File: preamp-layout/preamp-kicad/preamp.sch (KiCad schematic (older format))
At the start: 2 parts, among them SW1 Rotary_Encoder_Switch, SW2 Rotary_Encoder_Switch

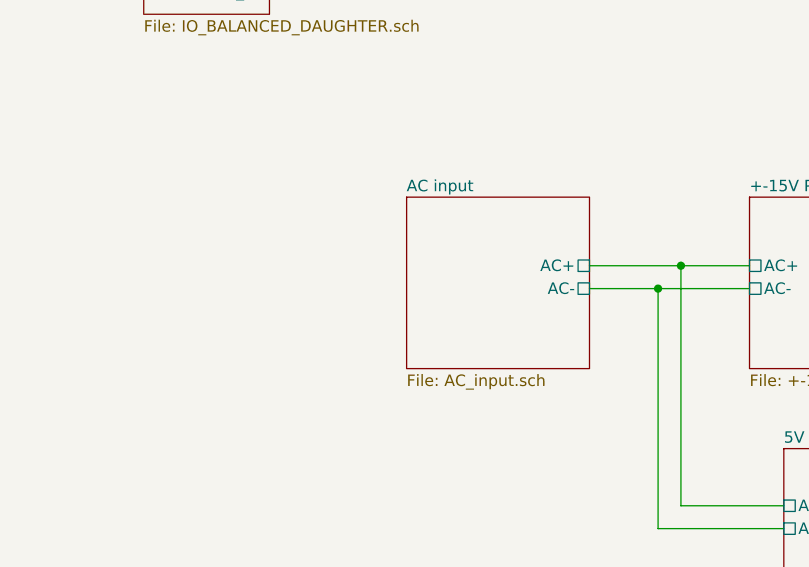
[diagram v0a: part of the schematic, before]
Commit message: AC PCB Update
Removed Switch symbol from PCB, moved to main sheet. Started playing with footprint assignment. Other minor updates.
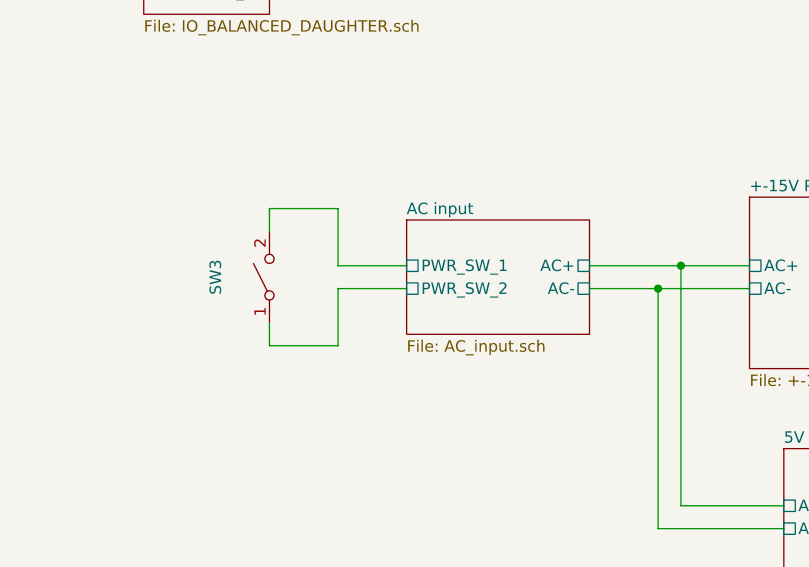
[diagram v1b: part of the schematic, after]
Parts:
- added SW3: SW_SPST, symbol Switch:SW_SPST
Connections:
- new net AC input/PWR_SW_1: SW3.2 (B)
- new net AC input/PWR_SW_2: SW3.1 (A)
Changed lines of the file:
@@
 $EndDescr
 $Sheet
-S 2550 5700 800  750
+S 2550 5800 800  500
 U 5E26F6FE
 F0 "AC input" 50
@@
 F2 "AC+" U R 3350 6000 50
 F3 "AC-" U R 3350 6100 50
+F4 "PWR_SW_1" U L 2550 6000 50
+F5 "PWR_SW_2" U L 2550 6100 50
 $EndSheet
 $Sheet
@@
 F4 "CLK" I R 5850 4150 50
 F5 "CS" I R 5850 4400 50
-F9 "LED_DT" I R 5850 4500 50
+F6 "LED_DT" I R 5850 4500 50
 $EndSheet
 $Sheet
@@
 Wire Wire Line
 	10750 2400 10750 2900
+$Comp
+L Switch:SW_SPST SW?
+U 1 1 5E2E8D21
+P 1950 6050
+AR Path="/5E26F6FE/5E2E8D21" Ref="SW?"  Part="1"
+AR Path="/5E2E8D21" Ref="SW3"  Part="1"
+F 0 "SW3" H 1950 6285 50  0000 C CNN
+F 1 "SW_SPST" H 1950 6194 50  0001 C CNN
+F 2 "" H 1950 6050 50  0001 C CNN
+F 3 "~" H 1950 6050 50  0001 C CNN
+	1    1950 6050
+	0    -1   -1   0
+$EndComp
+Wire Wire Line
+	1950 5850 1950 5750
+Wire Wire Line
+	1950 5750 2250 5750
+Wire Wire Line
+	2250 5750 2250 6000
+Wire Wire Line
+	2250 6000 2550 6000
+Wire Wire Line
+	1950 6250 1950 6350
+Wire Wire Line
+	1950 6350 2250 6350
+Wire Wire Line
+	2250 6350 2250 6100
+Wire Wire Line
+	2250 6100 2550 6100
 Wire Bus Line
 	5200 1700 5200 3300

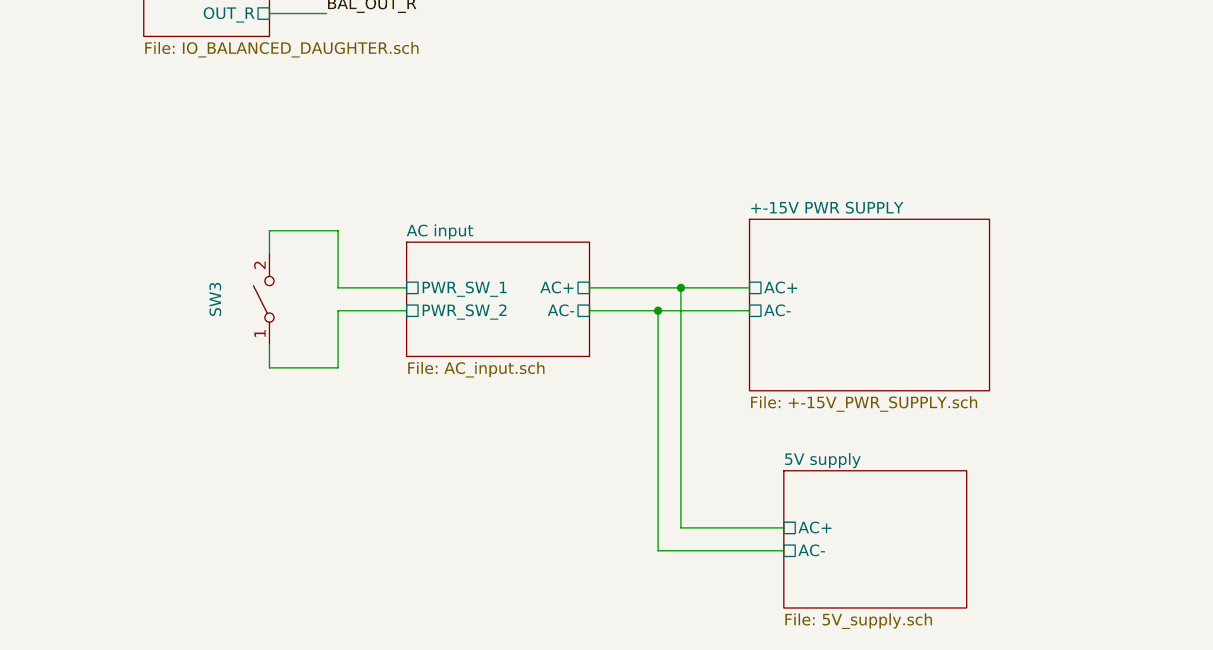
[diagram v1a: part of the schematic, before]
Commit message: Initial Footprint Assignment
Assigned footprints to SMT resistors, pin headers, screw terminals, LEDs, DIP-8 ICs
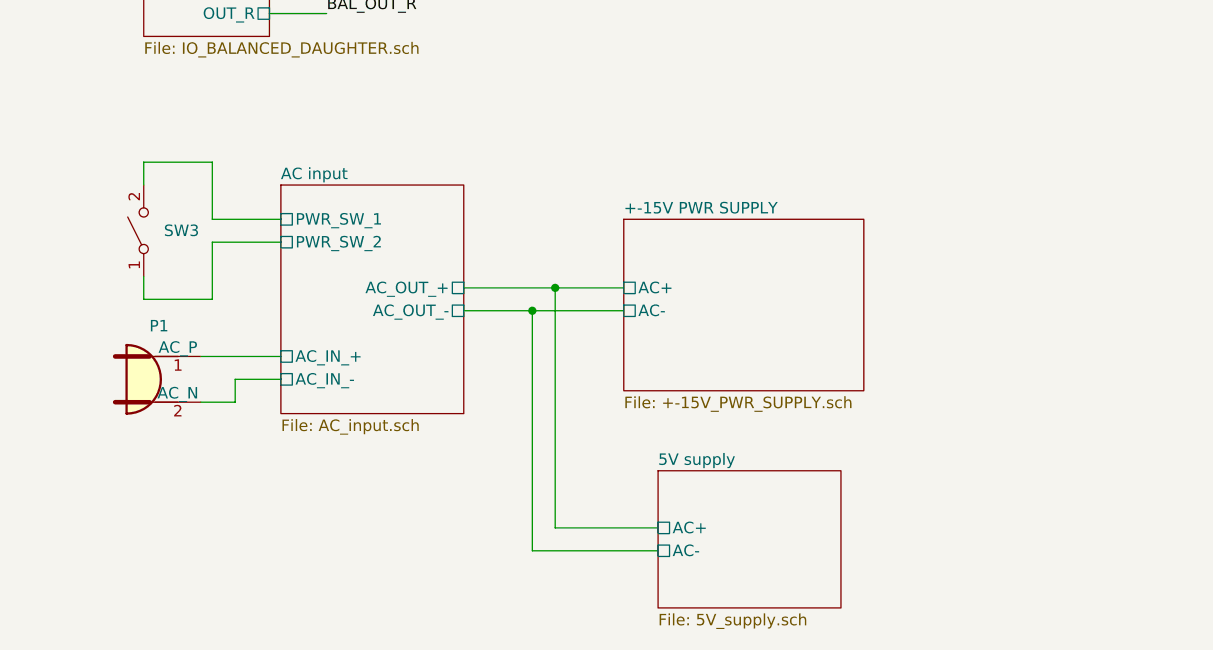
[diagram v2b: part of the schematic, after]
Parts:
- added P1: Conn_WallPlug, symbol Connector:Conn_WallPlug
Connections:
- new net AC input/AC_IN_+: P1.1 (AC_P)
- new net AC input/AC_IN_-: P1.2 (AC_N)
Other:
- moved on the sheet: SW3
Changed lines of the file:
@@
 $EndDescr
 $Sheet
-S 2550 5800 800  500
+S 2000 5550 800  1000
 U 5E26F6FE
 F0 "AC input" 50
 F1 "AC_input.sch" 50
-F2 "AC+" U R 3350 6000 50
-F3 "AC-" U R 3350 6100 50
-F4 "PWR_SW_1" U L 2550 6000 50
-F5 "PWR_SW_2" U L 2550 6100 50
-$EndSheet
-$Sheet
-S 4050 5700 1050 750
+F2 "PWR_SW_1" U L 2000 5700 50
+F3 "PWR_SW_2" U L 2000 5800 50
+F4 "AC_OUT_+" U R 2800 6000 50
+F5 "AC_IN_-" U L 2000 6400 50
+F6 "AC_IN_+" U L 2000 6300 50
+F7 "AC_OUT_-" U R 2800 6100 50
+$EndSheet
+$Sheet
+S 3500 5700 1050 750
 U 5E27B612
 F0 "+-15V PWR SUPPLY" 50
 F1 "+-15V_PWR_SUPPLY.sch" 50
-F2 "AC+" U L 4050 6000 50
-F3 "AC-" U L 4050 6100 50
-$EndSheet
-$Sheet
-S 4200 6800 800  600
+F2 "AC+" U L 3500 6000 50
+F3 "AC-" U L 3500 6100 50
+$EndSheet
+$Sheet
+S 3650 6800 800  600
 U 5E5EF2D4
 F0 "5V supply" 50
 F1 "5V_supply.sch" 50
-F2 "AC+" U L 4200 7050 50
-F3 "AC-" U L 4200 7150 50
+F2 "AC+" U L 3650 7050 50
+F3 "AC-" U L 3650 7150 50
 $EndSheet
 $Sheet
@@
 	8000 3500 8100 3600
 Wire Wire Line
-	3350 6000 3750 6000
-Wire Wire Line
-	3350 6100 3650 6100
-Wire Wire Line
-	3750 6000 3750 7050
-Wire Wire Line
-	3750 7050 4200 7050
-Connection ~ 3750 6000
-Wire Wire Line
-	3750 6000 4050 6000
-Wire Wire Line
-	3650 6100 3650 7150
-Wire Wire Line
-	3650 7150 4200 7150
-Connection ~ 3650 6100
-Wire Wire Line
-	3650 6100 4050 6100
+	2800 6000 3200 6000
+Wire Wire Line
+	2800 6100 3100 6100
+Wire Wire Line
+	3200 6000 3200 7050
+Wire Wire Line
+	3200 7050 3650 7050
+Connection ~ 3200 6000
+Wire Wire Line
+	3200 6000 3500 6000
+Wire Wire Line
+	3100 6100 3100 7150
+Wire Wire Line
+	3100 7150 3650 7150
+Connection ~ 3100 6100
+Wire Wire Line
+	3100 6100 3500 6100
 Wire Wire Line
 	1950 4450 2200 4450
@@
 L Switch:SW_SPST SW?
 U 1 1 5E2E8D21
-P 1950 6050
+P 1400 5750
 AR Path="/5E26F6FE/5E2E8D21" Ref="SW?"  Part="1"
 AR Path="/5E2E8D21" Ref="SW3"  Part="1"
-F 0 "SW3" H 1950 6285 50  0000 C CNN
-F 1 "SW_SPST" H 1950 6194 50  0001 C CNN
-F 2 "" H 1950 6050 50  0001 C CNN
-F 3 "~" H 1950 6050 50  0001 C CNN
-	1    1950 6050
+F 0 "SW3" V 1400 5662 50  0000 R CNN
+F 1 "SW_SPST" H 1400 5894 50  0001 C CNN
+F 2 "" H 1400 5750 50  0001 C CNN
+F 3 "~" H 1400 5750 50  0001 C CNN
+	1    1400 5750
 	0    -1   -1   0
 $EndComp
 Wire Wire Line
-	1950 5850 1950 5750
-Wire Wire Line
-	1950 5750 2250 5750
-Wire Wire Line
-	2250 5750 2250 6000
-Wire Wire Line
-	2250 6000 2550 6000
-Wire Wire Line
-	1950 6250 1950 6350
-Wire Wire Line
-	1950 6350 2250 6350
-Wire Wire Line
-	2250 6350 2250 6100
-Wire Wire Line
-	2250 6100 2550 6100
+	1400 5550 1400 5450
+Wire Wire Line
+	1400 5450 1700 5450
+Wire Wire Line
+	1700 5450 1700 5700
+Wire Wire Line
+	1700 5700 2000 5700
+Wire Wire Line
+	1400 5950 1400 6050
+Wire Wire Line
+	1400 6050 1700 6050
+Wire Wire Line
+	1700 6050 1700 5800
+Wire Wire Line
+	1700 5800 2000 5800
+$Comp
+L Connector:Conn_WallPlug P?
+U 1 1 5E300B43
+P 1450 6400
+AR Path="/5E26F6FE/5E300B43" Ref="P?"  Part="1"
+AR Path="/5E300B43" Ref="P1"  Part="1"
+F 0 "P1" H 1467 6633 50  0000 C CNN
+F 1 "Conn_WallPlug" H 1467 6634 50  0001 C CNN
+F 2 "" H 1850 6400 50  0001 C CNN
+F 3 "~" H 1850 6400 50  0001 C CNN
+	1    1450 6400
+	1    0    0    -1
+$EndComp
+Wire Wire Line
+	1650 6300 2000 6300
+Wire Wire Line
+	1650 6500 1800 6500
+Wire Wire Line
+	1800 6500 1800 6400
+Wire Wire Line
+	1800 6400 2000 6400
 Wire Bus Line
 	5200 1700 5200 3300

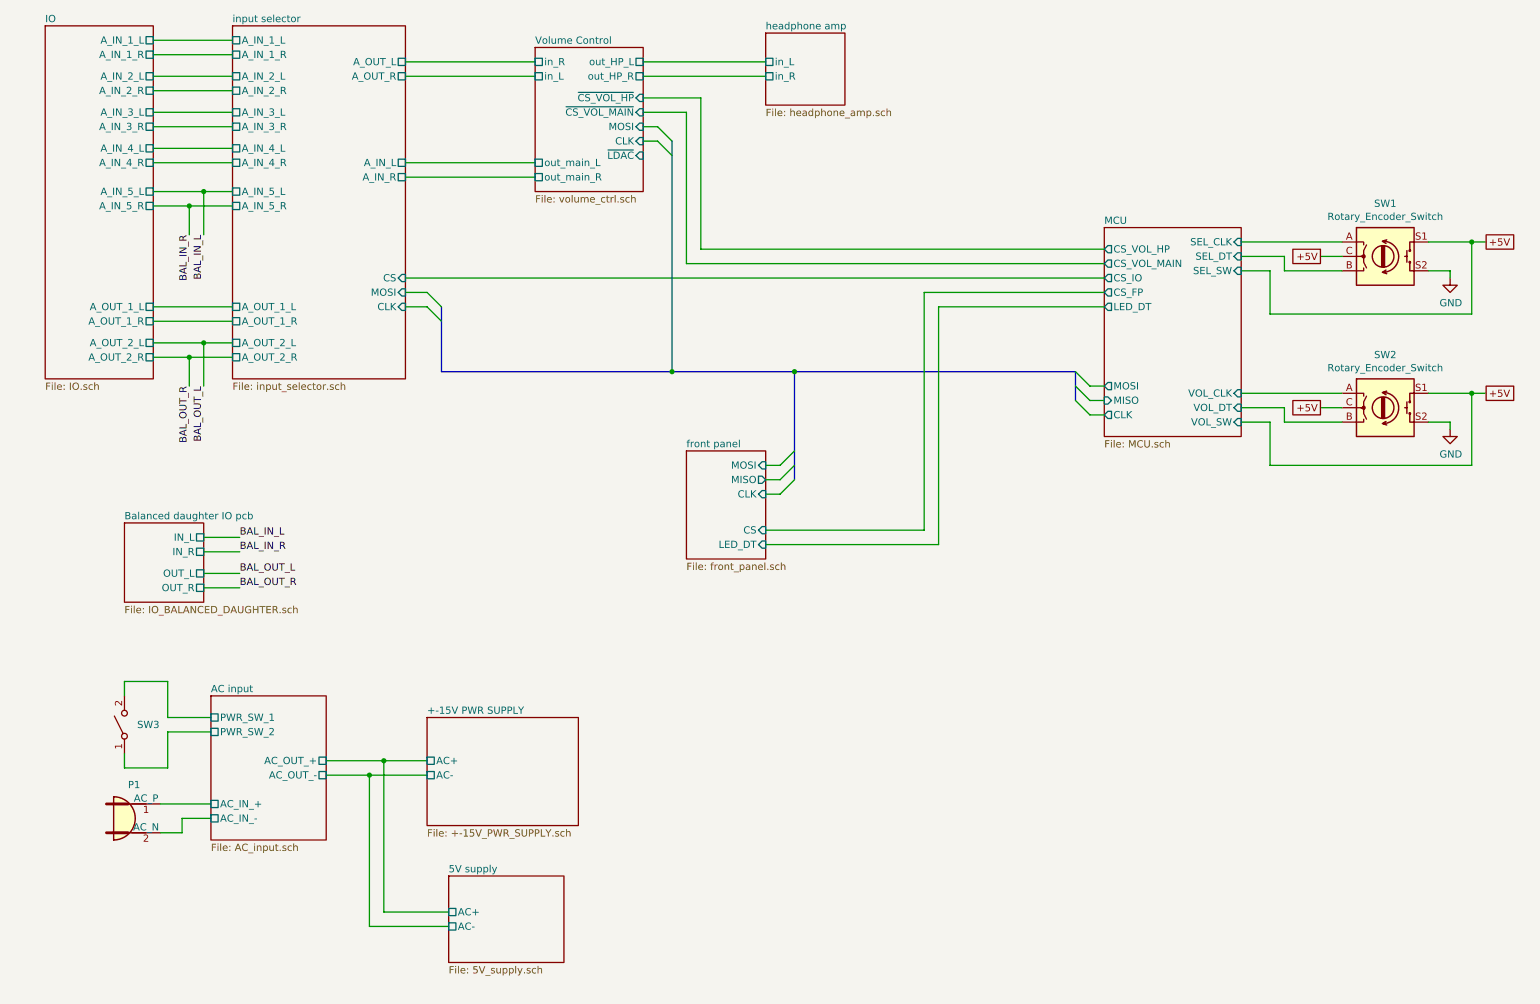
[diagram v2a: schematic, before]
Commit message: Added front panel LED sheet. BOM update. Front panel PCA work
other minor changes like LED color assignments, etc
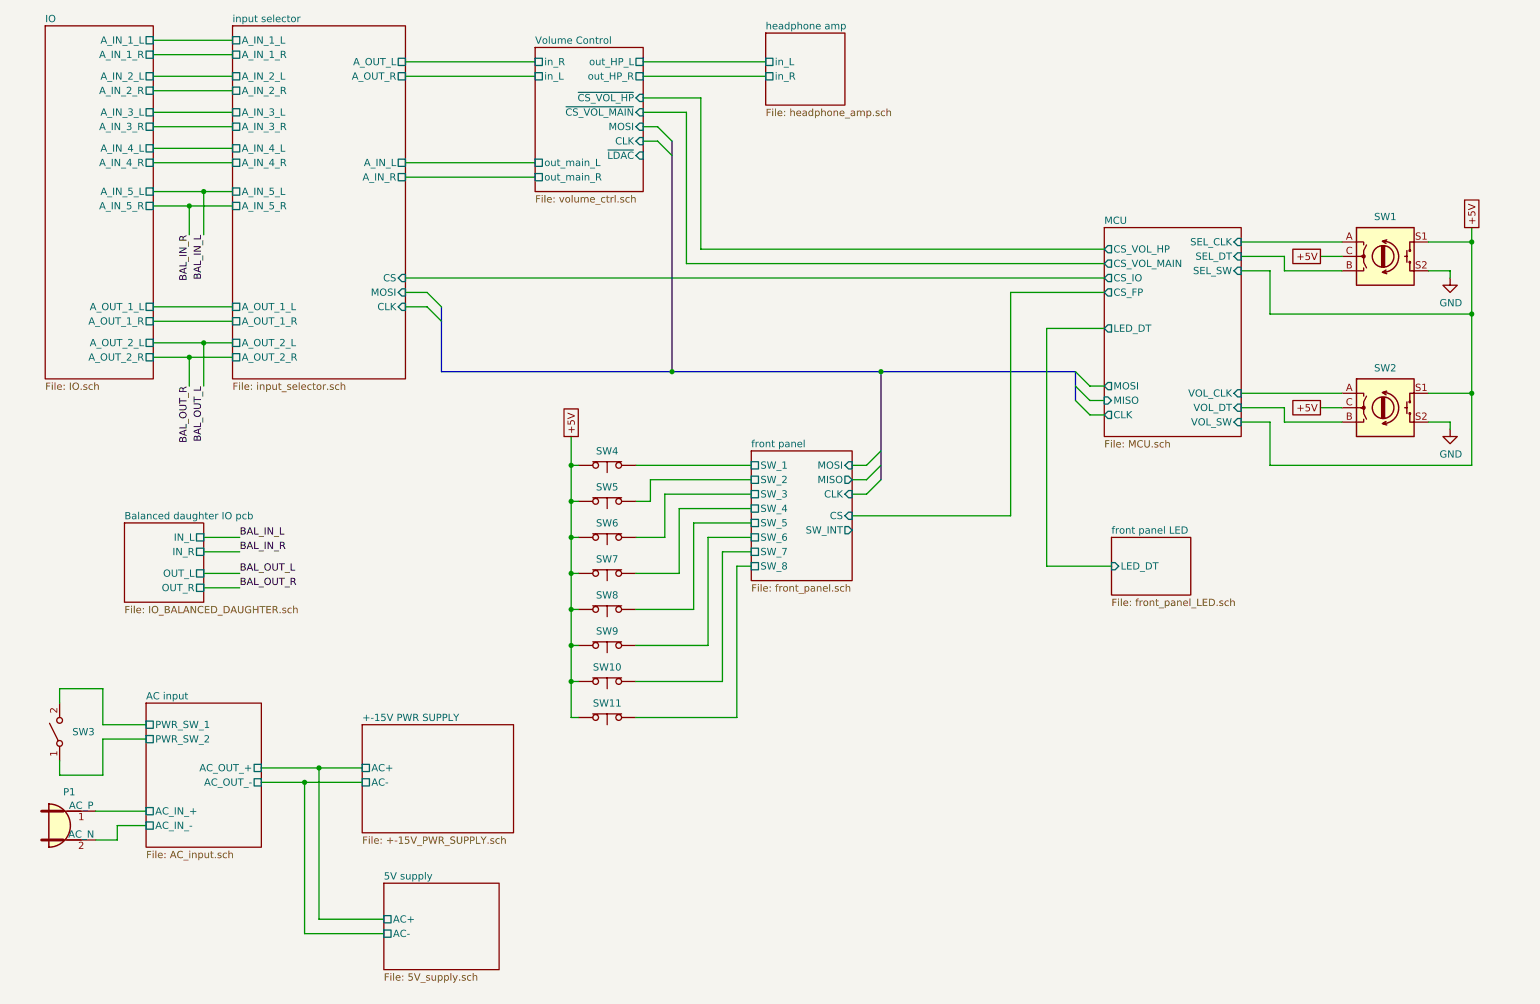
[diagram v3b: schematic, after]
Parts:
- added SW10, SW11, SW4, SW5, SW6, SW7, SW8, SW9: SW_Push_Open, symbol Switch:SW_Push_Open
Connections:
- net +5V: now also SW10.2 (B), SW11.2 (B), SW4.2 (B), SW5.2 (B), SW6.2 (B), SW7.2 (B), SW8.2 (B), SW9.2 (B)
- new net front panel/SW_1: SW4.1 (A)
- new net front panel/SW_2: SW5.1 (A)
- new net front panel/SW_3: SW6.1 (A)
- new net front panel/SW_4: SW7.1 (A)
- new net front panel/SW_5: SW8.1 (A)
- new net front panel/SW_6: SW9.1 (A)
- new net front panel/SW_7: SW10.1 (A)
- new net front panel/SW_8: SW11.1 (A)
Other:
- moved on the sheet: P1, SW3

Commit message: LED resistor update
In the process of reviewing layouts and associated parts sourcing, I realized that I had incorrectly calculated the resistors needed for the power supply LEDs on all boards. Updated BOM and schematics to match. Other minor schematic updates.
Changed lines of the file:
@@
 $EndSheet
 $Sheet
-S 3050 5750 1050 750
+S 3050 5950 550  300
 U 5E27B612
 F0 "+-15V PWR SUPPLY" 50
@@
 $EndSheet
 $Sheet
-S 3200 6850 800  600
+S 3200 7000 550  300
 U 5E5EF2D4
 F0 "5V supply" 50
@@
 	1350 6450 1550 6450
 $Sheet
-S 8250 4450 550  400
+S 8250 4500 550  300
 U 5E960098
 F0 "front panel LED" 50
@@
 Wire Wire Line
 	10750 2900 10750 3450
+Connection ~ 10750 2900
+Connection ~ 10750 3450
 Wire Bus Line
 	5200 1700 5200 3300
@@
 Wire Bus Line
 	6650 3300 6650 4050
-Connection ~ 10750 2900
-Connection ~ 10750 3450
 $EndSCHEMATC
